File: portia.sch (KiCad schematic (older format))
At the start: 53 parts, among them J1 Conn_01x02, J10 txrx, J11 i2s, J12 i2s, J16 Conn_01x04, J2 Conn_01x02, J3 sensor, J4 Conn_02x04_Counter_Clockwise, J5 Conn_02x04_Counter_Clockwise, J6 Conn_02x04_Counter_Clockwise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

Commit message: removed esd
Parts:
- removed C1: C_Small, Capacitor_SMD:C_0603_1608Metric_Pad1.05x0.95mm_HandSolder, symbol Device:C_Small
- removed D1, D2, D4, D5, D6: D_TVS, Diode_SMD:D_SOD-123F, symbol Device:D_TVS
- removed J16: Conn_01x04, Connector_PinHeader_2.54mm:PinHeader_1x04_P2.54mm_Vertical, symbol Connector_Generic:Conn_01x04
- removed J4: Conn_02x04_Counter_Clockwise, Connector_PinHeader_2.54mm:PinHeader_2x04_P2.54mm_Vertical, symbol Connector_Generic:Conn_02x04_Counter_Clockwise
- removed R3: R_Small, Resistor_SMD:R_0603_1608Metric_Pad1.05x0.95mm_HandSolder, symbol Device:R_Small
- added J13, J4: Conn_01x04, Connector_PinHeader_2.54mm:PinHeader_1x04_P2.54mm_Vertical, symbol Connector_Generic:Conn_01x04
- added J14: icsp, Connector_PinHeader_2.54mm:PinHeader_2x03_P2.54mm_Vertical, symbol Connector_Generic:Conn_02x03_Counter_Clockwise
- Y1: footprint Crystal:Crystal_SMD_0603-2Pin_6.0x3.5mm_HandSoldering -> Crystal:Crystal_SMD_G8-2Pin_3.2x1.5mm_HandSoldering
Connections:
- wire segments 213 -> 186
- no-connect marks 8 -> 9

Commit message: update layout
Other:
- moved on the sheet: J10
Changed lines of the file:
@@
 Wire Wire Line
 	9150 5300 9000 5300
-Text Label 11450 6150 0    50   ~ 0
-rxd0
 $Comp
 L power:+3.3V #PWR0102
@@
 	0    -1   -1   0
 $EndComp
-Text Label 11450 6050 0    50   ~ 0
-txd0
 Wire Wire Line
 	8600 5400 8250 5400
@@
 L Connector_Generic:Conn_01x02 J10
 U 1 1 5C67FC32
-P 11950 5350
-F 0 "J10" H 12030 5342 50  0000 L CNN
-F 1 "txrx" H 11950 5150 50  0000 L CNN
-F 2 "Connector_PinHeader_2.54mm:PinHeader_1x02_P2.54mm_Vertical" H 11950 5350 50  0001 C CNN
-F 3 "~" H 11950 5350 50  0001 C CNN
-	1    11950 5350
+P 11650 6050
+F 0 "J10" H 11730 6042 50  0000 L CNN
+F 1 "txrx" H 11650 5850 50  0000 L CNN
+F 2 "Connector_PinHeader_2.54mm:PinHeader_1x02_P2.54mm_Vertical" H 11650 6050 50  0001 C CNN
+F 3 "~" H 11650 6050 50  0001 C CNN
+	1    11650 6050
 	1    0    0    -1
 $EndComp
@@
 Text Label 11400 4550 1    50   ~ 0
 scl
+Text Label 18300 7100 0    50   ~ 0
+sda
 Text Label 18300 7000 0    50   ~ 0
-sda
-Text Label 18300 7100 0    50   ~ 0
 scl
 $Comp
@@
 L Connector:USB_B_Micro J8
 U 1 1 5C6C2176
-P 15350 2400
-F 0 "J8" H 15121 2298 50  0000 R CNN
-F 1 "USB_B_Micro" H 15121 2389 50  0000 R CNN
-F 2 "Connector_USB:USB_Micro-B_Amphenol_10103594-0001LF_Horizontal" H 15500 2350 50  0001 C CNN
-F 3 "~" H 15500 2350 50  0001 C CNN
-	1    15350 2400
-	-1   0    0    1
-$EndComp
-Text Label 14000 2300 2    50   ~ 0
+P 14250 3500
+F 0 "J8" H 14021 3398 50  0000 R CNN
+F 1 "USB_B_Micro" H 14021 3489 50  0000 R CNN
+F 2 "Connector_USB:USB_Micro-B_Amphenol_10103594-0001LF_Horizontal" H 14400 3450 50  0001 C CNN
+F 3 "~" H 14400 3450 50  0001 C CNN
+	1    14250 3500
+	-1   0    0    1
+$EndComp
+Text Label 12900 3400 2    50   ~ 0
 usb_tx_-
-Text Label 14000 2400 2    50   ~ 0
+Text Label 12900 3500 2    50   ~ 0
 usb_rx_+
 Wire Wire Line
-	15350 2000 15350 1550
+	14250 3100 14250 2650
 $Comp
 L power:GND #PWR0117
 U 1 1 5C71FB50
-P 15350 1550
-F 0 "#PWR0117" H 15350 1300 50  0001 C CNN
-F 1 "GND" H 15355 1377 50  0000 C CNN
-F 2 "" H 15350 1550 50  0001 C CNN
-F 3 "" H 15350 1550 50  0001 C CNN
-	1    15350 1550
+P 14250 2650
+F 0 "#PWR0117" H 14250 2400 50  0001 C CNN
+F 1 "GND" H 14255 2477 50  0000 C CNN
+F 2 "" H 14250 2650 50  0001 C CNN
+F 3 "" H 14250 2650 50  0001 C CNN
+	1    14250 2650
 	-1   0    0    1
 $EndComp
@@
 L power:+3.3V #PWR0119
 U 1 1 5C88E71E
-P 14550 2600
-F 0 "#PWR0119" H 14550 2450 50  0001 C CNN
-F 1 "+3.3V" V 14565 2728 50  0000 L CNN
-F 2 "" H 14550 2600 50  0001 C CNN
-F 3 "" H 14550 2600 50  0001 C CNN
-	1    14550 2600
+P 13450 3700
+F 0 "#PWR0119" H 13450 3550 50  0001 C CNN
+F 1 "+3.3V" V 13465 3828 50  0000 L CNN
+F 2 "" H 13450 3700 50  0001 C CNN
+F 3 "" H 13450 3700 50  0001 C CNN
+	1    13450 3700
 	0    -1   -1   0
 $EndComp
@@
 Wire Wire Line
 	14250 5500 14550 5500
-$Comp
-L Connector_Generic:Conn_02x04_Counter_Clockwise J6
-U 1 1 5CC730A6
-P 14750 6400
-F 0 "J6" H 14800 6717 50  0000 C CNN
-F 1 "Conn_02x04_Counter_Clockwise" H 14800 6626 50  0000 C CNN
-F 2 "Connector_PinHeader_2.54mm:PinHeader_2x04_P2.54mm_Vertical" H 14750 6400 50  0001 C CNN
-F 3 "~" H 14750 6400 50  0001 C CNN
-	1    14750 6400
-	1    0    0    -1
-$EndComp
 Wire Wire Line
 	15050 6300 16750 6300
@@
 	15050 6600 16750 6600
 Wire Wire Line
-	16750 6700 14550 6700
-Wire Wire Line
-	14550 6700 14550 6600
-Wire Wire Line
-	16750 6800 14450 6800
-Wire Wire Line
-	14450 6800 14450 6500
-Wire Wire Line
-	14450 6500 14550 6500
-Wire Wire Line
-	16750 6900 14350 6900
-Wire Wire Line
-	14350 6900 14350 6400
-Wire Wire Line
-	14350 6400 14550 6400
-Wire Wire Line
 	16750 7000 14250 7000
-Wire Wire Line
-	14250 7000 14250 6300
-Wire Wire Line
-	14250 6300 14550 6300
 $Comp
 L Device:Crystal_Small Y1
@@
 	12000 6550 12450 6550
 Wire Wire Line
-	14000 2300 15050 2300
-Wire Wire Line
-	14000 2400 15050 2400
-Wire Wire Line
-	15050 2600 14550 2600
-NoConn ~ 15450 2000
+	12900 3400 13950 3400
+Wire Wire Line
+	12900 3500 13950 3500
+Wire Wire Line
+	13950 3700 13450 3700
+NoConn ~ 14350 3100
+Wire Wire Line
+	16750 6900 14350 6900
+Wire Wire Line
+	16750 6800 14450 6800
+Wire Wire Line
+	16750 6700 14550 6700
+Wire Wire Line
+	14550 6700 14550 6600
+Wire Wire Line
+	14250 7000 14250 6300
+Wire Wire Line
+	14350 6900 14350 6400
+Wire Wire Line
+	14350 6400 14550 6400
+Wire Wire Line
+	14250 6300 14550 6300
+Wire Wire Line
+	14450 6500 14550 6500
+Wire Wire Line
+	14450 6800 14450 6500
+$Comp
+L Connector_Generic:Conn_02x04_Counter_Clockwise J6
+U 1 1 5CC730A6
+P 14750 6400
+F 0 "J6" H 14800 6717 50  0000 C CNN
+F 1 "Conn_02x04_Counter_Clockwise" H 14800 6626 50  0000 C CNN
+F 2 "Connector_PinHeader_2.54mm:PinHeader_2x04_P2.54mm_Vertical" H 14750 6400 50  0001 C CNN
+F 3 "~" H 14750 6400 50  0001 C CNN
+	1    14750 6400
+	1    0    0    -1
+$EndComp
+Text Label 11750 5450 0    50   ~ 0
+rxd0
+Text Label 11750 5350 0    50   ~ 0
+txd0
 $EndSCHEMATC

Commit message: update layout
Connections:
- net labels added: _N, _P
- net labels removed: usb_rx_+, usb_tx_-
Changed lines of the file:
@@
 $EndComp
 Text Label 16400 7600 2    50   ~ 0
-usb_rx_+
+_P
 Text Label 16400 7500 2    50   ~ 0
-usb_tx_-
+_N
 $Comp
 L Connector:USB_B_Micro J8
@@
 $EndComp
 Text Label 12900 3400 2    50   ~ 0
-usb_tx_-
+_N
 Text Label 12900 3500 2    50   ~ 0
-usb_rx_+
+_P
 Wire Wire Line
 	14250 3100 14250 2650

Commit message: redesign
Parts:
- removed C10: 10uf, Capacitor_SMD:CP_Elec_4x4.5, symbol Device:CP1
- removed C11, C12, C13, C14, C2, C3, C4, C5, C6, C7: C_Small, Capacitor_SMD:C_0603_1608Metric_Pad1.05x0.95mm_HandSolder, symbol Device:C_Small
- removed C8: C0.1uf, Capacitor_SMD:C_0603_1608Metric, symbol Device:C
- removed C9: 10uf, Capacitor_SMD:CP_Elec_4x5.3, symbol Device:CP1
- removed D3: LED_ARGB, LED_SMD:LED_RGB_1210, symbol Device:LED_ARGB
- removed H2, H3, H4, H6, H8: MountingHole, MountingHole:MountingHole_3mm, symbol Mechanical:MountingHole
- removed J1, J2: Conn_01x02, Connector_PinHeader_2.54mm:PinHeader_1x02_P2.54mm_Vertical, symbol Connector_Generic:Conn_01x02
- removed J10: txrx, Connector_PinHeader_2.54mm:PinHeader_1x02_P2.54mm_Vertical, symbol Connector_Generic:Conn_01x02
- removed J11, J12: i2s, Connector_PinHeader_2.54mm:PinHeader_1x02_P2.54mm_Vertical, symbol Connector_Generic:Conn_01x02
- removed J13, J4: Conn_01x04, Connector_PinHeader_2.54mm:PinHeader_1x04_P2.54mm_Vertical, symbol Connector_Generic:Conn_01x04
- removed J14: icsp, Connector_PinHeader_2.54mm:PinHeader_2x03_P2.54mm_Vertical, symbol Connector_Generic:Conn_02x03_Counter_Clockwise
- removed J3: sensor, Connector_PinHeader_2.54mm:PinHeader_1x02_P2.54mm_Vertical, symbol Connector_Generic:Conn_01x02
- removed J5, J6: Conn_02x04_Counter_Clockwise, Connector_PinHeader_2.54mm:PinHeader_2x04_P2.54mm_Vertical, symbol Connector_Generic:Conn_02x04_Counter_Clockwise
- removed J7: vin, Connector_PinHeader_2.54mm:PinHeader_1x02_P2.54mm_Vertical, symbol Connector_Generic:Conn_01x02
- removed J8: USB_B_Micro, Connector_USB:USB_Micro-B_Amphenol_10103594-0001LF_Horizontal, symbol Connector:USB_B_Micro
- removed J9: dac, Connector_PinHeader_2.54mm:PinHeader_1x02_P2.54mm_Vertical, symbol Connector_Generic:Conn_01x02
- removed R1, R2, R4: 10k, Resistor_SMD:R_0603_1608Metric_Pad1.05x0.95mm_HandSolder, symbol Device:R_Small
- removed R11, R18: 75, Resistor_SMD:R_0603_1608Metric, symbol Device:R
- removed R19: 100, Resistor_SMD:R_0603_1608Metric, symbol Device:R
- removed U1: ATSAMD51J20A-AU, ATSAMD51J20A-AU:QFP50P1200X1200X120-64N, symbol ATSAMD51J20A-AU:ATSAMD51J20A-AU
- removed U5: LM1117-3.3, Package_TO_SOT_SMD:SOT-223, symbol Regulator_Linear:LM1117-3.3
- removed Y1: Crystal_Small, Crystal:Crystal_SMD_G8-2Pin_3.2x1.5mm_HandSoldering, symbol Device:Crystal_Small
- added J? (x2): Conn_02x03_Counter_Clockwise, symbol Connector_Generic:Conn_02x03_Counter_Clockwise
- added J? (x2): Conn_01x04, symbol Connector_Generic:Conn_01x04
- added R?: R10K, Resistor_SMD:R_0603_1608Metric, symbol Device:R
- added SW?: Reset, Button_Switch_SMD:SW_SPST_EVPBF, symbol Switch:SW_Push
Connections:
- net labels removed: RESET, VCC, _N, _P, rxd0, scl, sda, txd0
- wire segments 186 -> 64
- no-connect marks 9 -> 1
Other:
- moved on the sheet: H5, R6

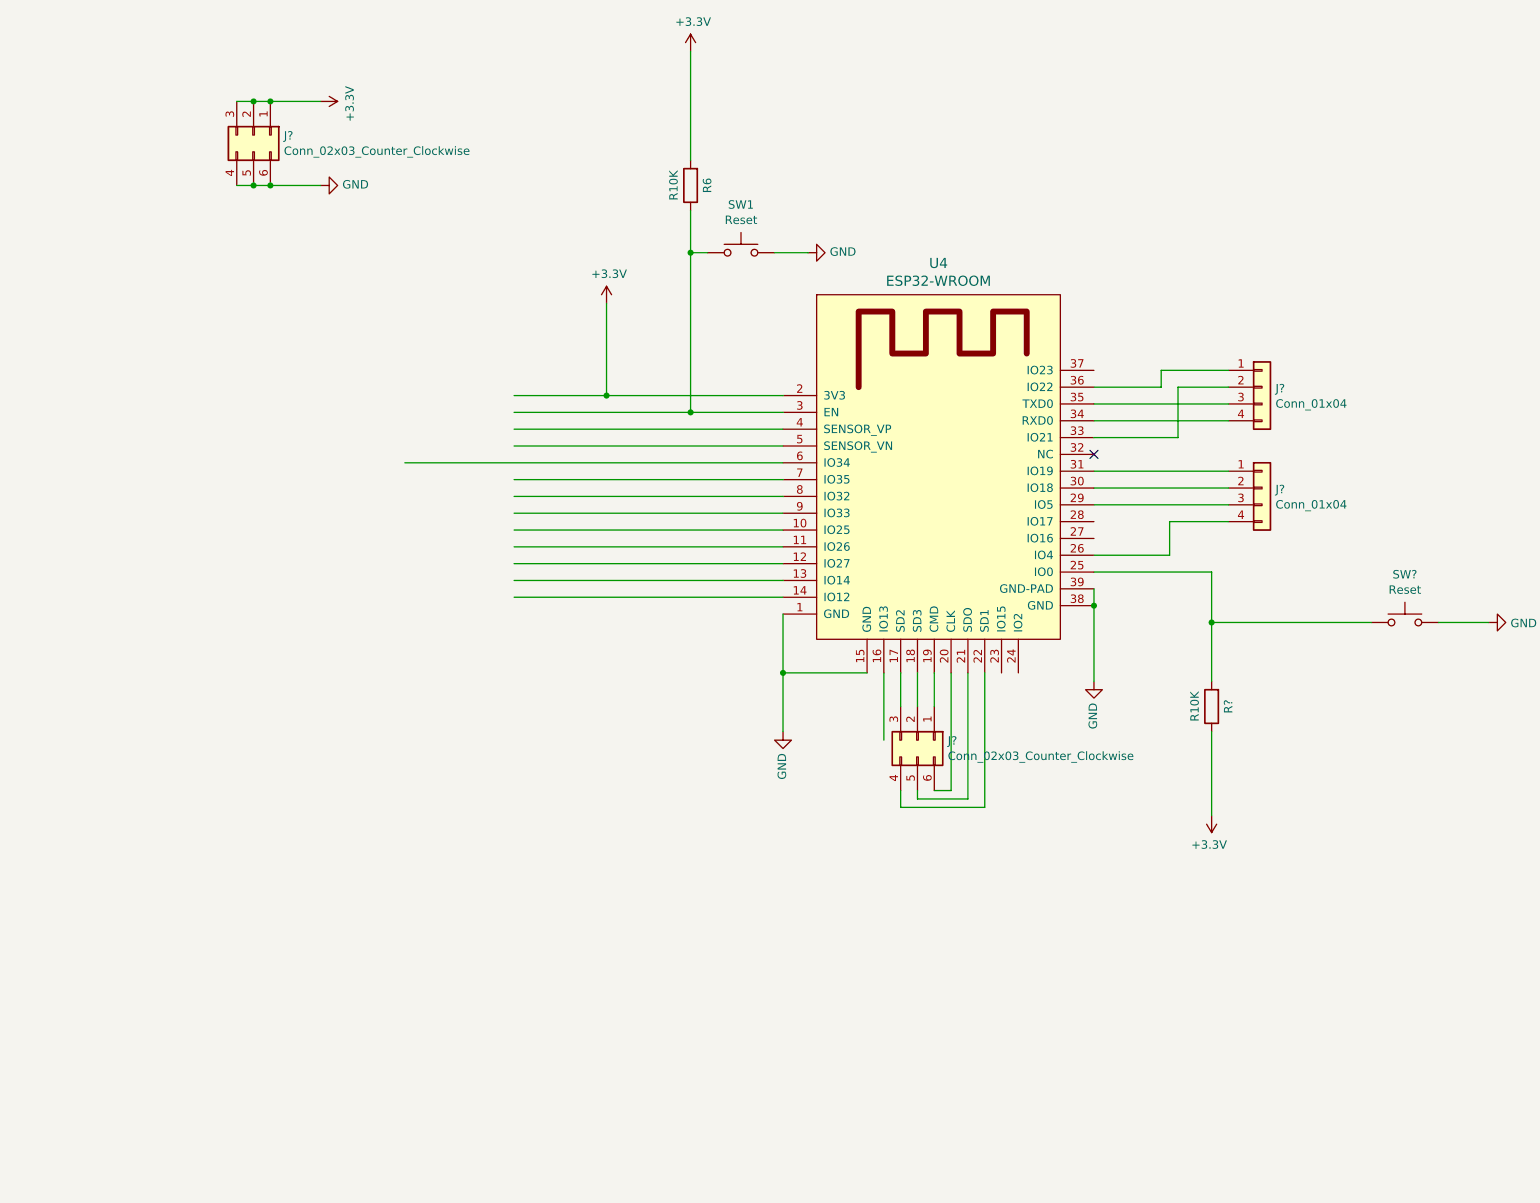
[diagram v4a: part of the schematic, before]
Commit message: update schematic
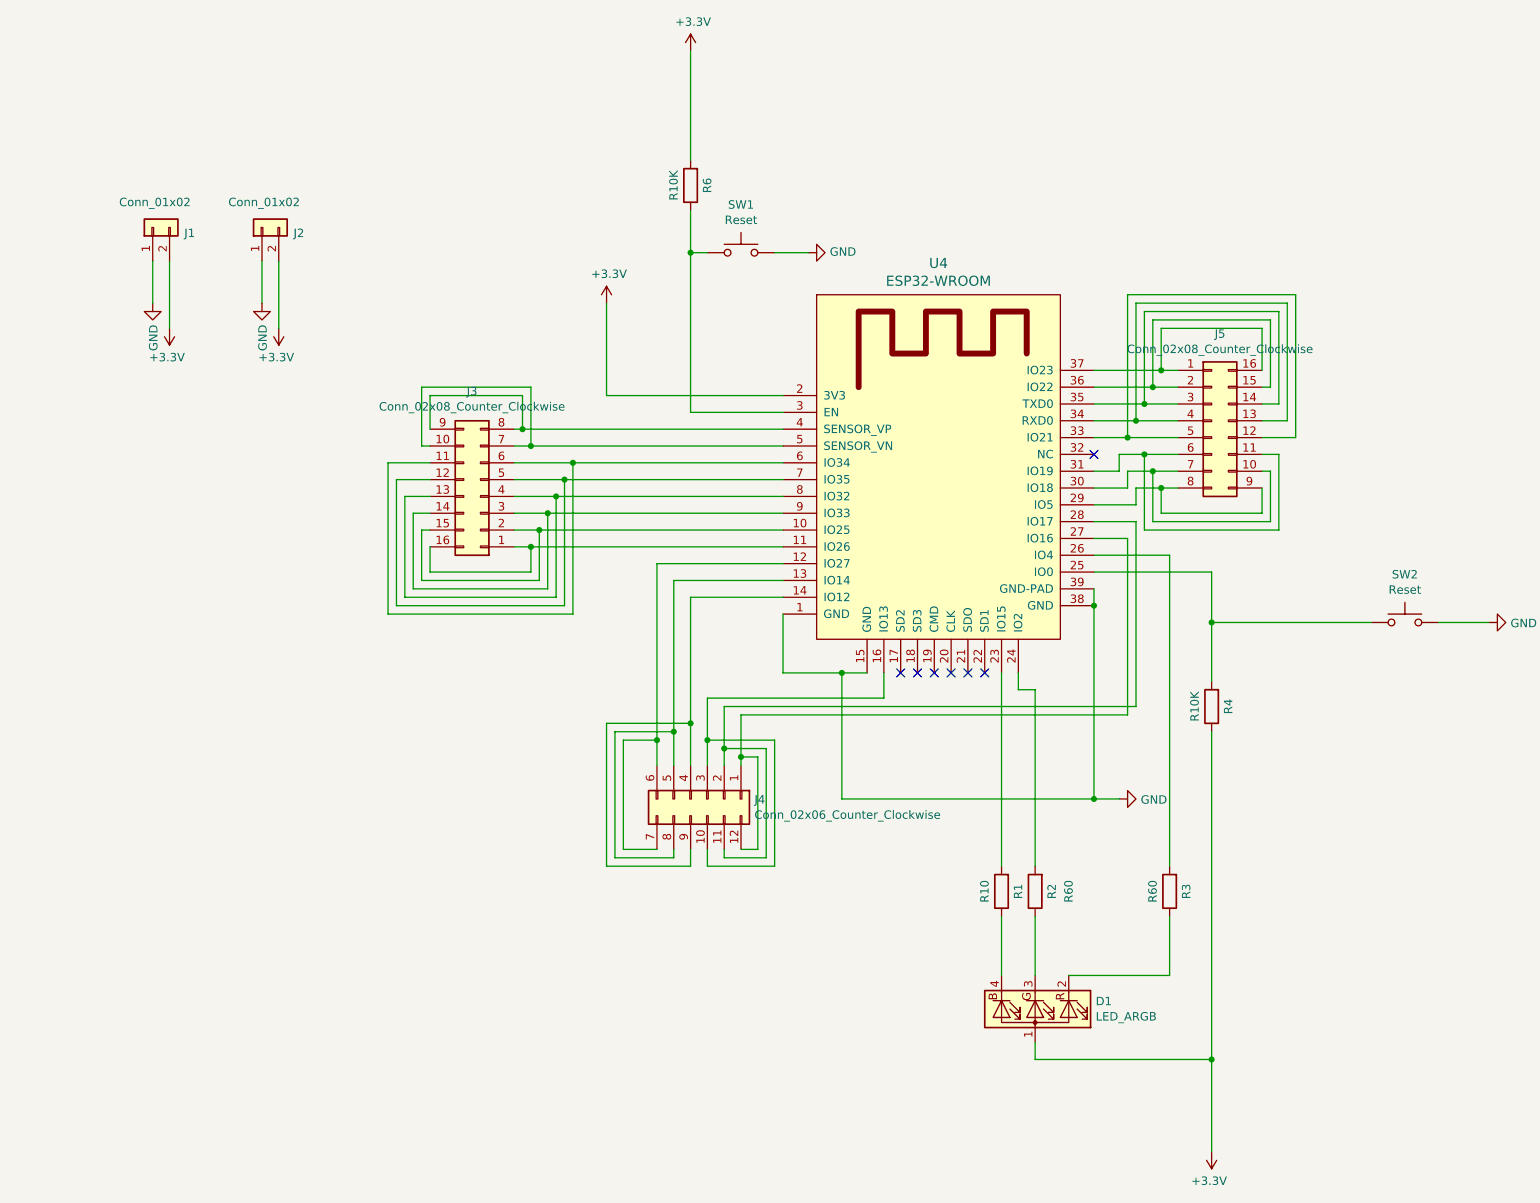
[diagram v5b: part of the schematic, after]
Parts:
- removed J? (x2): Conn_02x03_Counter_Clockwise, symbol Connector_Generic:Conn_02x03_Counter_Clockwise
- removed J? (x2): Conn_01x04, symbol Connector_Generic:Conn_01x04
- added D1: LED_ARGB, LED_SMD:LED_RGB_1210, symbol Device:LED_ARGB
- added J1, J2: Conn_01x02, Connector_PinHeader_2.54mm:PinHeader_1x02_P2.54mm_Vertical, symbol Connector_Generic:Conn_01x02
- added J3, J5: Conn_02x08_Counter_Clockwise, Connector_PinHeader_2.54mm:PinHeader_2x08_P2.54mm_Vertical, symbol Connector_Generic:Conn_02x08_Counter_Clockwise
- added J4: Conn_02x06_Counter_Clockwise, Connector_PinHeader_2.54mm:PinHeader_2x08_P2.54mm_Vertical, symbol Connector_Generic:Conn_02x06_Counter_Clockwise
- added R1: R10, Resistor_SMD:R_0603_1608Metric, symbol Device:R
- added R2, R3: R60, Resistor_SMD:R_0603_1608Metric, symbol Device:R
- SW1: footprint Button_Switch_SMD:SW_SPST_EVPBF -> Button_Switch_SMD:SW_SPST_B3U-1000P-B
- SW2: renamed from SW?; footprint Button_Switch_SMD:SW_SPST_EVPBF -> Button_Switch_SMD:SW_SPST_B3U-1000P-B
- gave numbers to parts that had none: 1
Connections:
- wire segments 64 -> 182
- no-connect marks 1 -> 7

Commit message: update layout
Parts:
- J4: footprint Connector_PinHeader_2.54mm:PinHeader_2x08_P2.54mm_Vertical -> Connector_PinHeader_2.54mm:PinHeader_2x06_P2.54mm_Vertical
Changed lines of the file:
@@
 F 0 "J4" V 8704 7980 50  0000 L CNN
 F 1 "Conn_02x06_Counter_Clockwise" V 8795 7980 50  0000 L CNN
-F 2 "Connector_PinHeader_2.54mm:PinHeader_2x08_P2.54mm_Vertical" H 8700 7700 50  0001 C CNN
+F 2 "Connector_PinHeader_2.54mm:PinHeader_2x06_P2.54mm_Vertical" H 8700 7700 50  0001 C CNN
 F 3 "~" H 8700 7700 50  0001 C CNN
 	1    8700 7700

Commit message: layout redesign
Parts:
- removed J3, J5: Conn_02x08_Counter_Clockwise, Connector_PinHeader_2.54mm:PinHeader_2x08_P2.54mm_Vertical, symbol Connector_Generic:Conn_02x08_Counter_Clockwise
- removed J4: Conn_02x06_Counter_Clockwise, Connector_PinHeader_2.54mm:PinHeader_2x06_P2.54mm_Vertical, symbol Connector_Generic:Conn_02x06_Counter_Clockwise
- added J3, J5: Conn_02x08_Odd_Even, Connector_PinHeader_2.54mm:PinHeader_2x08_P2.54mm_Vertical, symbol Connector_Generic:Conn_02x08_Odd_Even
- added J?: Conn_02x06_Odd_Even, symbol Connector_Generic:Conn_02x06_Odd_Even
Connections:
- net at U4.10 (IO25): now also J3.13 (Pin_13), J3.14 (Pin_14)
- net at U4.11 (IO26): now also J3.15 (Pin_15), J3.16 (Pin_16)
- net at U4.12 (IO27): now also J?.1 (Pin_1), J?.2 (Pin_2)
- net at U4.13 (IO14): now also J?.3 (Pin_3), J?.4 (Pin_4)
- net at U4.14 (IO12): now also J?.5 (Pin_5), J?.6 (Pin_6)
- net at U4.16 (IO13): now also J?.7 (Pin_7), J?.8 (Pin_8)
- net at U4.27 (IO16): now also J?.11 (Pin_11), J?.12 (Pin_12)
- net at U4.28 (IO17): now also J?.10 (Pin_10), J?.9 (Pin_9)
- net at U4.29 (IO5): now also J5.1 (Pin_1), J5.2 (Pin_2)
- net at U4.30 (IO18): now also J5.3 (Pin_3), J5.4 (Pin_4)
- net at U4.31 (IO19): now also J5.5 (Pin_5), J5.6 (Pin_6)
- net at U4.33 (IO21): now also J5.7 (Pin_7), J5.8 (Pin_8)
- net at U4.34 (RXD0): now also J5.10 (Pin_10), J5.9 (Pin_9)
- net at U4.35 (TXD0): now also J5.11 (Pin_11), J5.12 (Pin_12)
- net at U4.36 (IO22): now also J5.13 (Pin_13), J5.14 (Pin_14)
- net at U4.37 (IO23): now also J5.15 (Pin_15), J5.16 (Pin_16)
- net at U4.4 (SENSOR_VP): now also J3.1 (Pin_1), J3.2 (Pin_2)
- net at U4.5 (SENSOR_VN): now also J3.3 (Pin_3), J3.4 (Pin_4)
- net at U4.6 (IO34): now also J3.5 (Pin_5), J3.6 (Pin_6)
- net at U4.7 (IO35): now also J3.7 (Pin_7), J3.8 (Pin_8)
- net at U4.8 (IO32): now also J3.10 (Pin_10), J3.9 (Pin_9)
- net at U4.9 (IO33): now also J3.11 (Pin_11), J3.12 (Pin_12)
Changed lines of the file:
@@
 Wire Wire Line
 	11000 6250 11450 6250
-$Comp
-L Connector_Generic:Conn_02x08_Counter_Clockwise J5
-U 1 1 5C71AF98
-P 11700 5450
-F 0 "J5" H 11750 5967 50  0000 C CNN
-F 1 "Conn_02x08_Counter_Clockwise" H 11750 5876 50  0000 C CNN
-F 2 "Connector_PinHeader_2.54mm:PinHeader_2x08_P2.54mm_Vertical" H 11700 5450 50  0001 C CNN
-F 3 "~" H 11700 5450 50  0001 C CNN
-	1    11700 5450
-	1    0    0    -1
-$EndComp
 Wire Wire Line
 	11000 5150 11400 5150
@@
 Wire Wire Line
 	12100 5650 12000 5650
-$Comp
-L Connector_Generic:Conn_02x08_Counter_Clockwise J3
-U 1 1 5C79F09B
-P 7350 5900
-F 0 "J3" H 7400 5275 50  0000 C CNN
-F 1 "Conn_02x08_Counter_Clockwise" H 7400 5366 50  0000 C CNN
-F 2 "Connector_PinHeader_2.54mm:PinHeader_2x08_P2.54mm_Vertical" H 7350 5900 50  0001 C CNN
-F 3 "~" H 7350 5900 50  0001 C CNN
-	1    7350 5900
-	-1   0    0    1
-$EndComp
 Wire Wire Line
 	9150 5700 7900 5700
@@
 Wire Wire Line
 	7650 5600 9150 5600
-$Comp
-L Connector_Generic:Conn_02x06_Counter_Clockwise J4
-U 1 1 5C84F180
-P 8700 7700
-F 0 "J4" V 8704 7980 50  0000 L CNN
-F 1 "Conn_02x06_Counter_Clockwise" V 8795 7980 50  0000 L CNN
-F 2 "Connector_PinHeader_2.54mm:PinHeader_2x06_P2.54mm_Vertical" H 8700 7700 50  0001 C CNN
-F 3 "~" H 8700 7700 50  0001 C CNN
-	1    8700 7700
-	0    1    1    0
-$EndComp
 Wire Wire Line
 	9150 6300 8400 6300
@@
 Wire Wire Line
 	11000 7700 11150 7700
+$Comp
+L Connector_Generic:Conn_02x08_Odd_Even J3
+U 1 1 5C751B37
+P 7250 5800
+F 0 "J3" H 7300 6317 50  0000 C CNN
+F 1 "Conn_02x08_Odd_Even" H 7300 6226 50  0000 C CNN
+F 2 "Connector_PinHeader_2.54mm:PinHeader_2x08_P2.54mm_Vertical" H 7250 5800 50  0001 C CNN
+F 3 "~" H 7250 5800 50  0001 C CNN
+	1    7250 5800
+	1    0    0    -1
+$EndComp
+$Comp
+L Connector_Generic:Conn_02x08_Odd_Even J5
+U 1 1 5C75C447
+P 11800 5550
+F 0 "J5" H 11850 4925 50  0000 C CNN
+F 1 "Conn_02x08_Odd_Even" H 11850 5016 50  0000 C CNN
+F 2 "Connector_PinHeader_2.54mm:PinHeader_2x08_P2.54mm_Vertical" H 11800 5550 50  0001 C CNN
+F 3 "~" H 11800 5550 50  0001 C CNN
+	1    11800 5550
+	-1   0    0    1
+$EndComp
+$Comp
+L Connector_Generic:Conn_02x06_Odd_Even J?
+U 1 1 5C7B3D0C
+P 8600 7800
+F 0 "J?" V 8696 7412 50  0000 R CNN
+F 1 "Conn_02x06_Odd_Even" V 8605 7412 50  0000 R CNN
+F 2 "" H 8600 7800 50  0001 C CNN
+F 3 "~" H 8600 7800 50  0001 C CNN
+	1    8600 7800
+	0    -1   -1   0
+$EndComp
 $EndSCHEMATC
